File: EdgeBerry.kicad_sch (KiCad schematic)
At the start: 25 parts, among them P1 12Vin, Q1 BC547, Q2 BC547, Q3 BC547, SW1 SW_PUSH, U1 24LC256, U2 LM2596

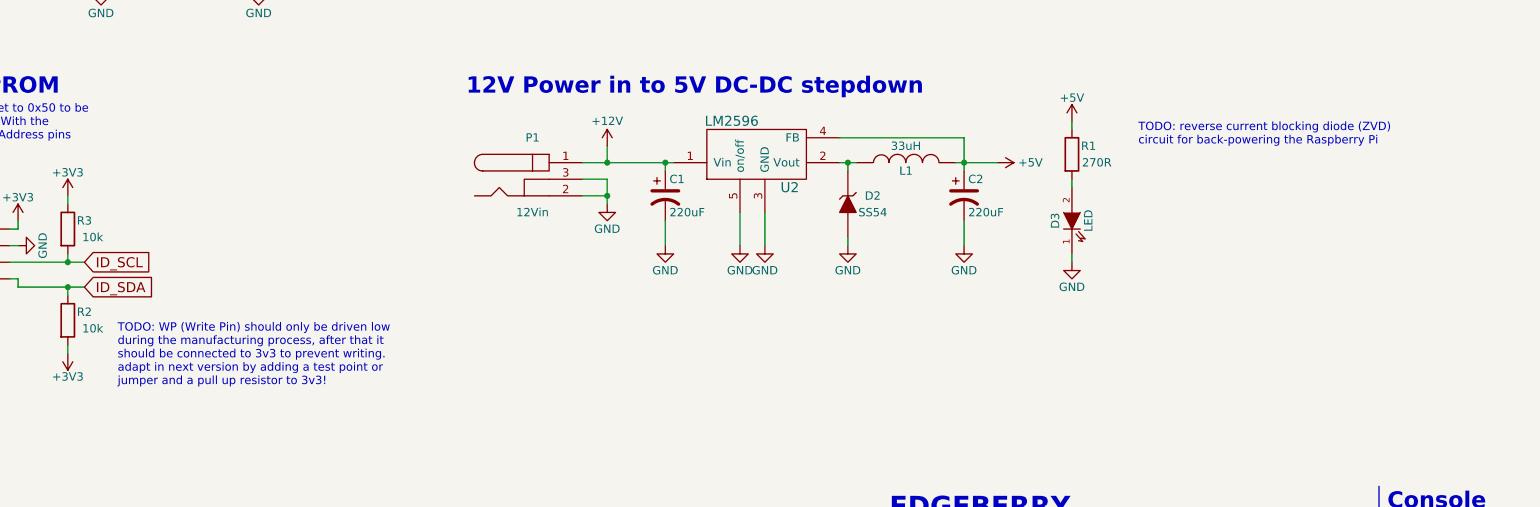
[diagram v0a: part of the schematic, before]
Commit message: Schematic: in-schematic todo's moved to GitHub issues
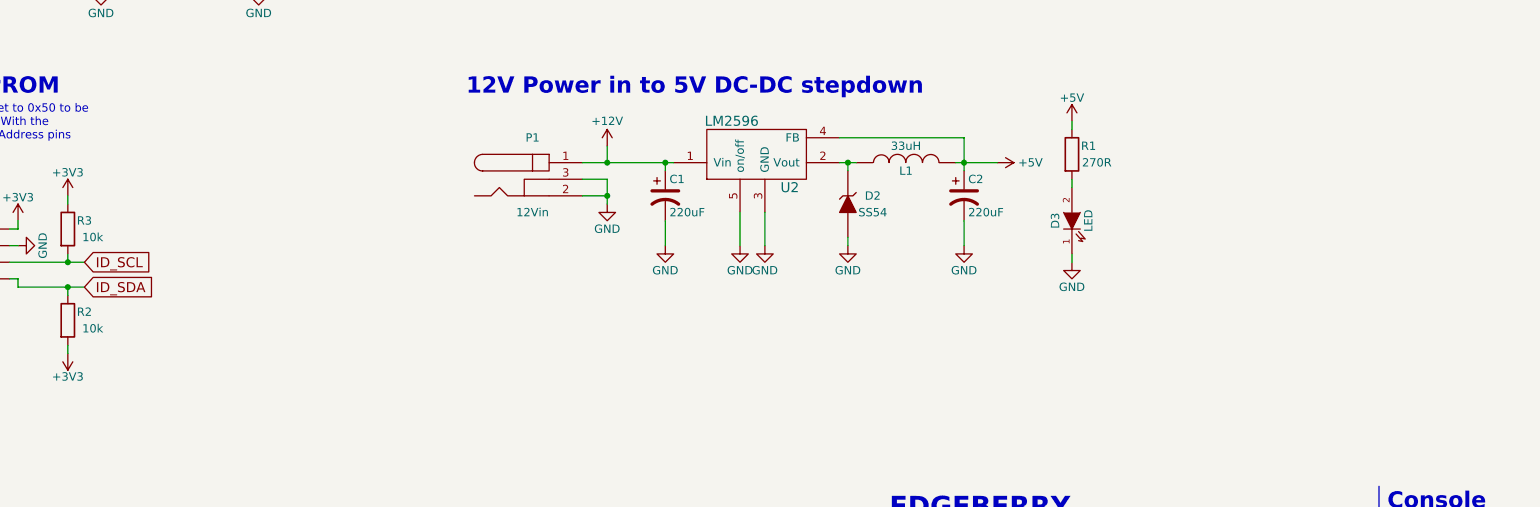
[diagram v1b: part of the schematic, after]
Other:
- note removed: "TODO: WP (Write Pin) should only be driven low during the manufacturing process, after that it should be connected to 3v3 to prevent writing. adapt in next version by adding a test point or jumper and a pull up resistor to 3v3!"
- note removed: "TODO: reverse current blocking diode (ZVD) circuit for back-powering the Raspberry Pi"
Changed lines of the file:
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@@
     (effects (font (size 2.4892 2.4892) (thickness 0.4978) bold) (justify left bottom))
-  )
-  (text "TODO: reverse current blocking diode (ZVD)\ncircuit for back-powering the Raspberry Pi"
-    (at 219.71 114.3 0)
-    (effects (font (size 1.27 1.27)) (justify left bottom))
   )
   (text "RPi Hat ID EEPROM" (at 17.78 106.68 0)
@@
     (effects (font (size 1.524 1.524)) (justify left bottom))
   )
-  (text "TODO: WP (Write Pin) should only be driven low\nduring the manufacturing process, after that it\nshould be connected to 3v3 to prevent writing.\nadapt in next version by adding a test point or\njumper and a pull up resistor to 3v3!"
-    (at 63.5 151.13 0)
-    (effects (font (size 1.27 1.27)) (justify left bottom))
-  )
   (text "EDGEBERRY" (at 181.61 171.45 0)

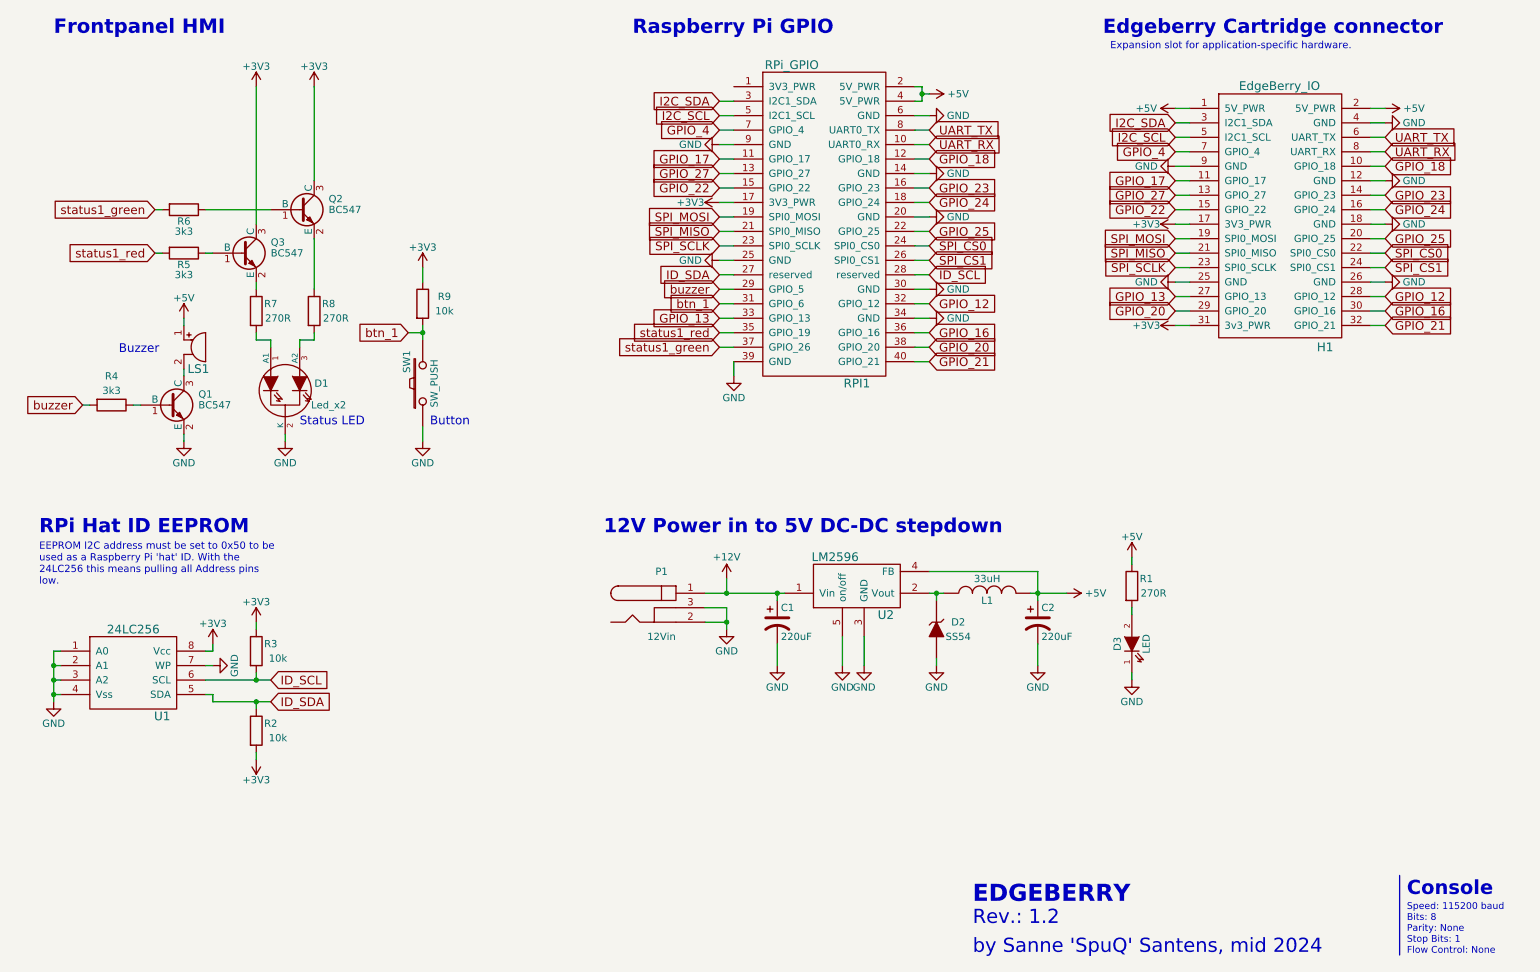
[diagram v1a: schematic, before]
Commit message: Schematic: cleanup + increased readability
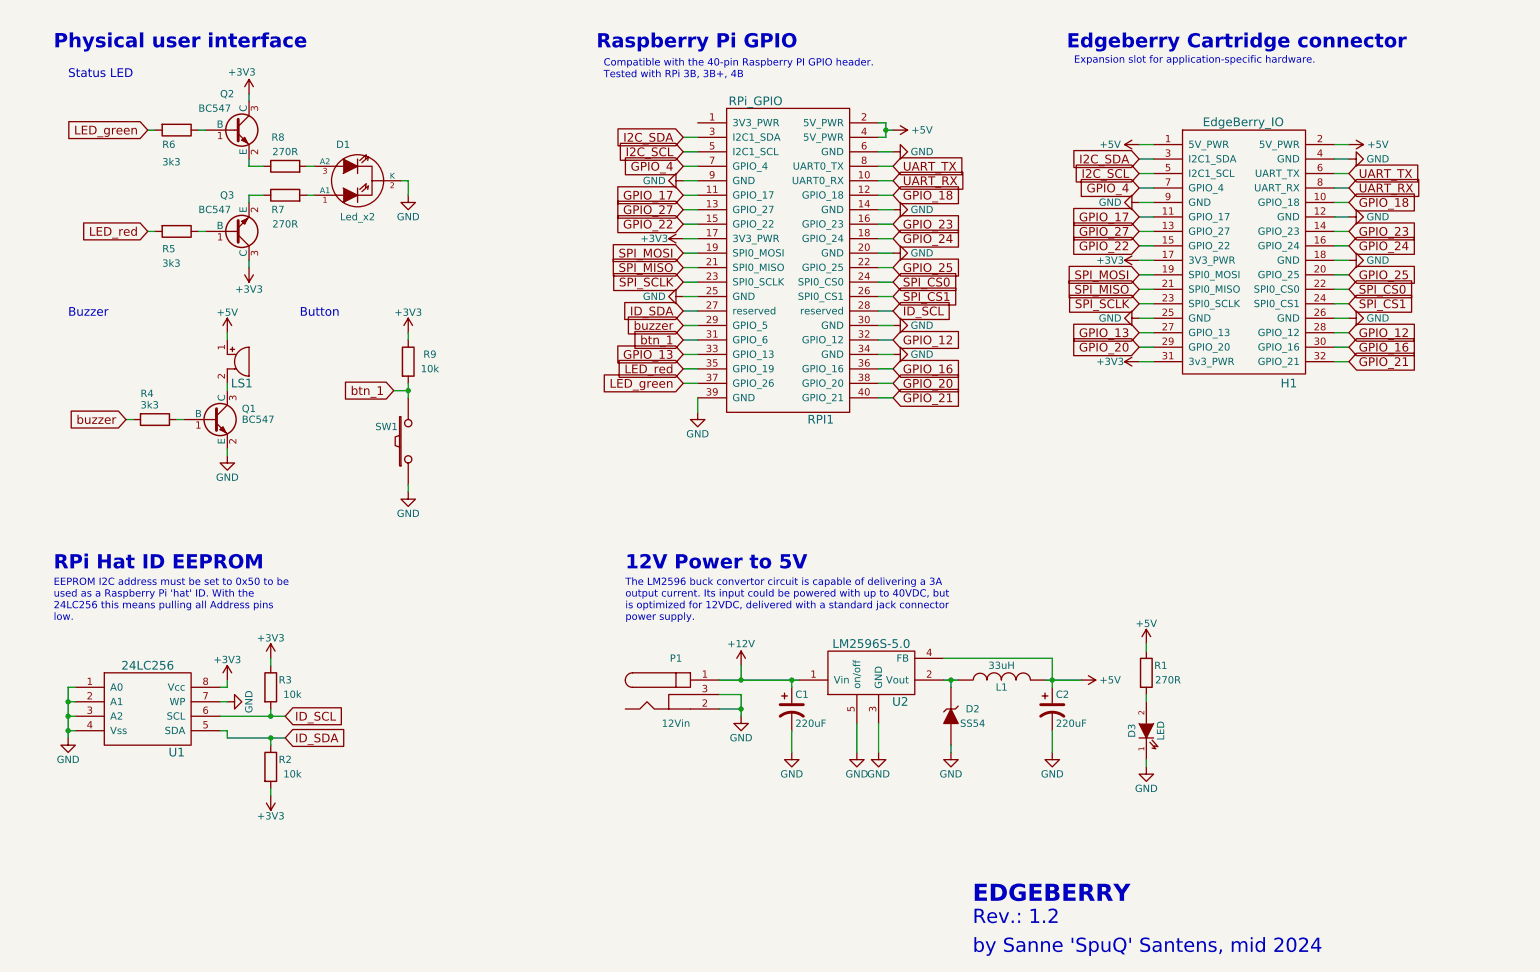
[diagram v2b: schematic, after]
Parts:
- U2: value LM2596 -> LM2596S-5.0
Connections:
- net status1_green renamed LED_green
- net status1_red renamed LED_red
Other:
- note added: "12V Power to 5V"
- note added: "Compatible with the 40-pin Raspberry PI GPIO header. Tested with RPi 3B, 3B+, 4B"
- note added: "Physical user interface"
- note added: "The LM2596 buck convertor circuit is capable of delivering a 3A output current. Its input could be powered with up to 40VDC, but is optimized for 12VDC, delivered with a standard jack connector power supply."
- note removed: "12V Power in to 5V DC-DC stepdown"
- note removed: "Console"
- note removed: "Frontpanel HMI"
- note removed: "Speed: 115200 baud Bits: 8 Parity: None Stop Bits: 1 Flow Control: None"
- title: (none) -> Edgeberry Hardware
- moved on the sheet: C1, C2, D1, D2, D3, H1, L1, LS1, P1, Q1, Q2, Q3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

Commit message: Schematic: cleanup + increased readability
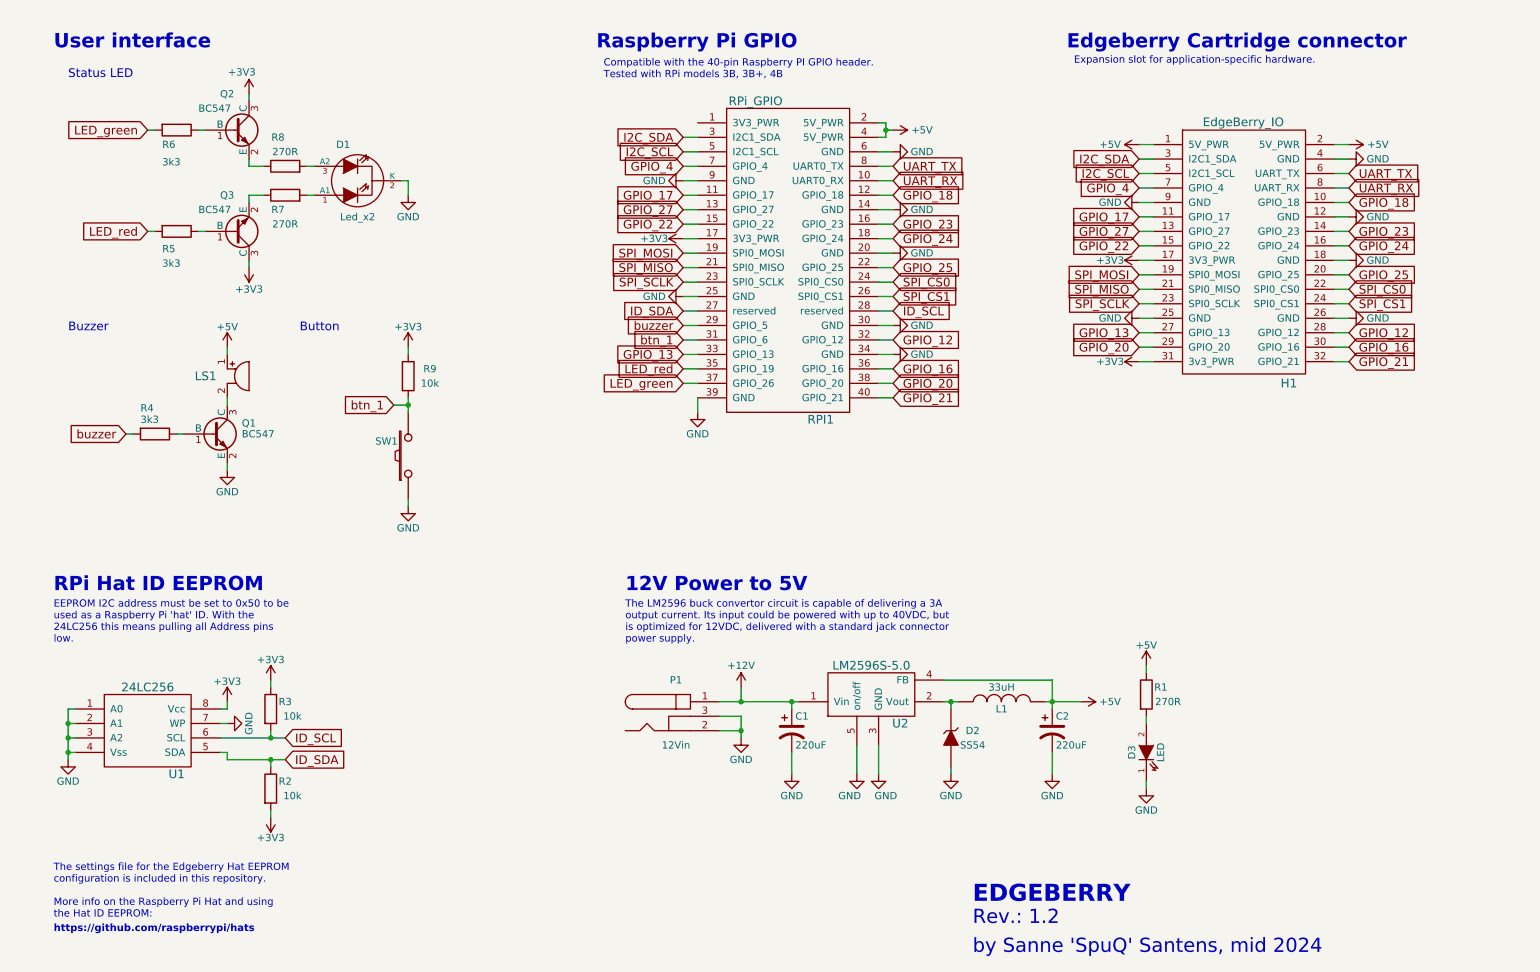
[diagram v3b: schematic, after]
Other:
- note added: "Compatible with the 40-pin Raspberry PI GPIO header. Tested with RPi models 3B, 3B+, 4B"
- note added: "The settings file for the Edgeberry Hat EEPROM configuration is included in this repository. More info on the Raspberry Pi Hat and using the Hat ID EEPROM:"
- note added: "User interface"
- note added: "https://github.com/raspberrypi/hats"
- note removed: "Compatible with the 40-pin Raspberry PI GPIO header. Tested with RPi 3B, 3B+, 4B"
- note removed: "Physical user interface"
- moved on the sheet: C1, C2, D2, D3, L1, LS1, P1, Q1, R1, R2, R3, R4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
